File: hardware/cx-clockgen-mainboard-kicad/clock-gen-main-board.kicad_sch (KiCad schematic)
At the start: 19 parts, among them J1 Conn_01x03_Pin, J2 Conn_01x03_Pin, J3 Headswitch_SMA, J4 Conn_01x01_Pin, J5 Conn_01x01_Pin, J6 Conn_01x01_Pin, J7 Conn_01x01_Pin, J8 Conn_Coaxial, U1 Pico

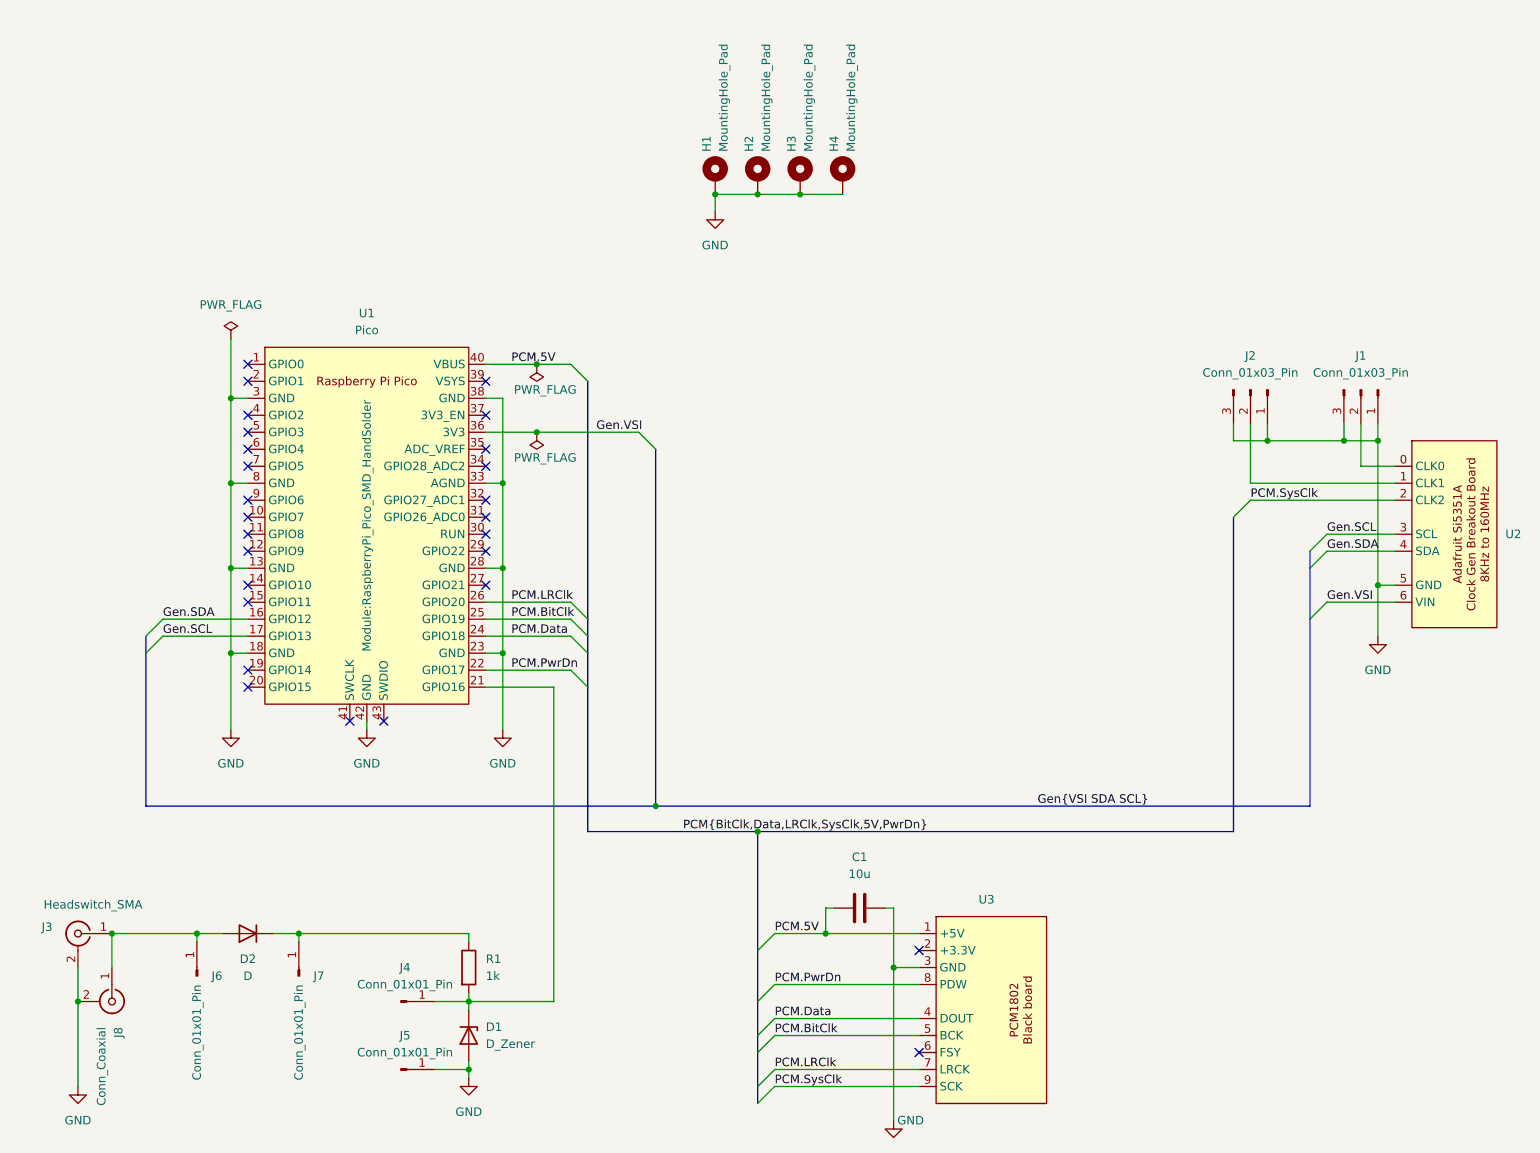
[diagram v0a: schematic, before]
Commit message: Added missing setup shell scripts
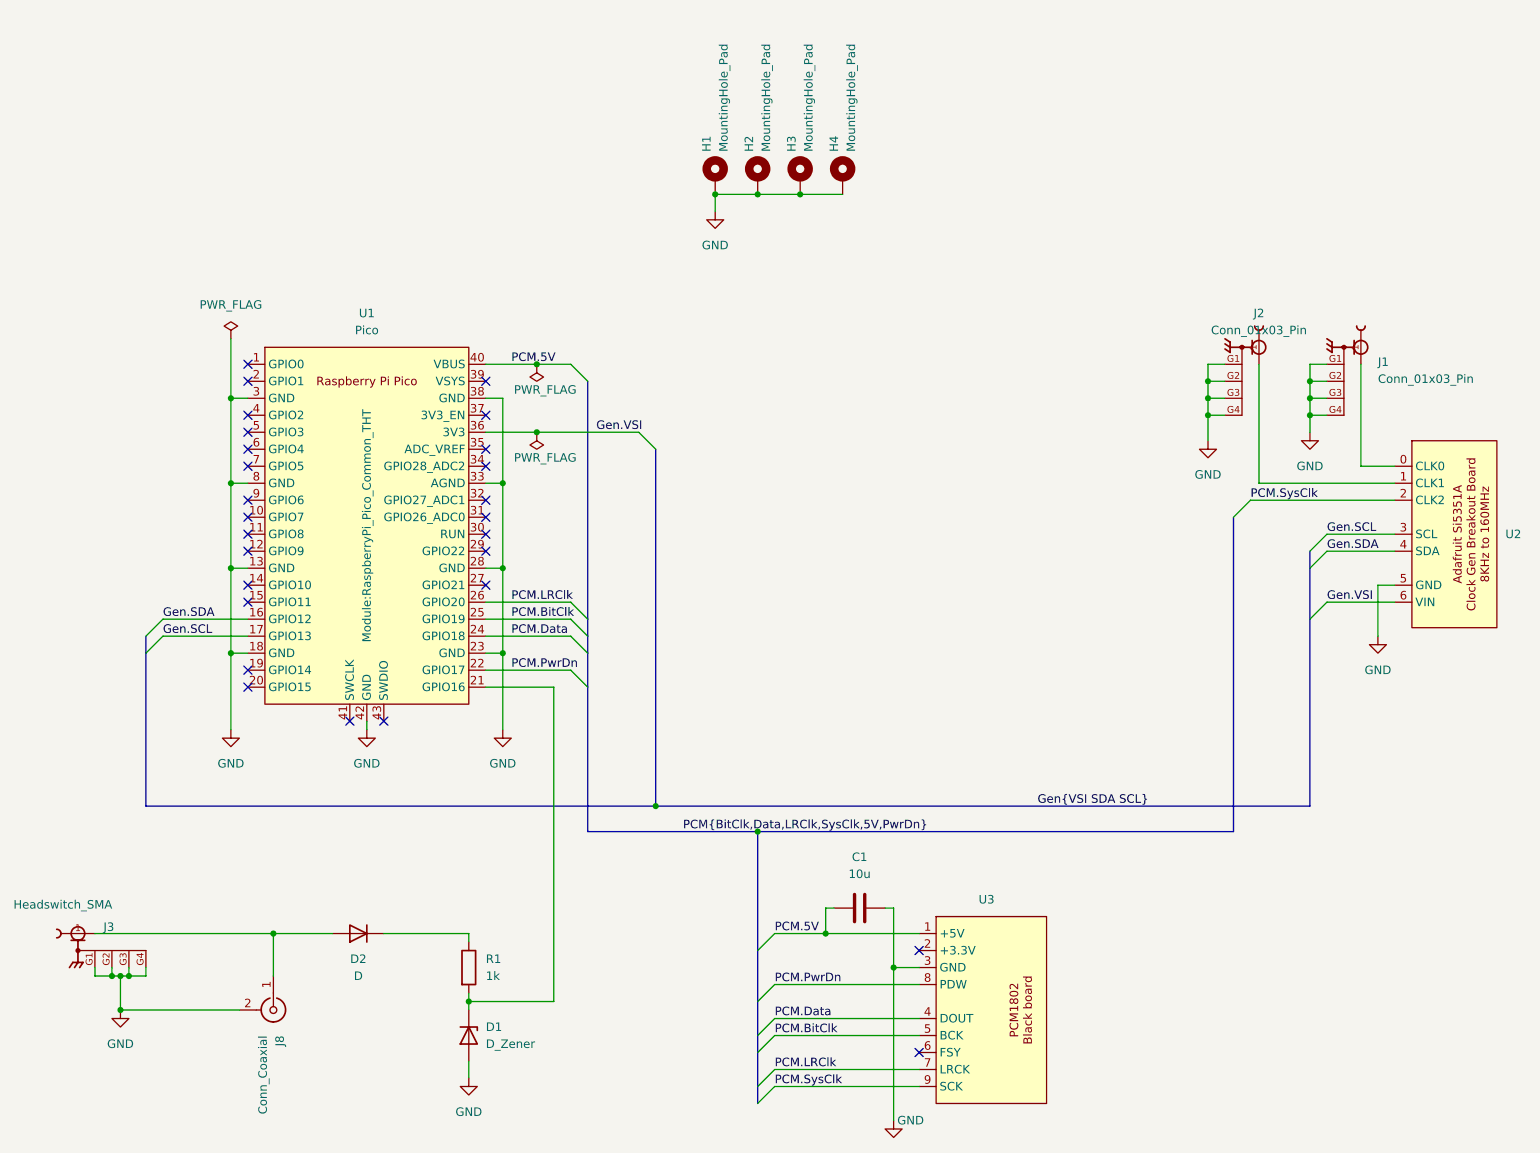
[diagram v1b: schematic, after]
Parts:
- removed J4, J5, J6, J7: Conn_01x01_Pin, Connector_PinHeader_2.54mm:PinHeader_1x01_P2.54mm_Vertical, symbol Connector:Conn_01x01_Pin
- J1, J2: footprint Connector_PinHeader_2.54mm:PinHeader_1x03_P2.54mm_Vertical -> Clockgen Footprints:GRADCONN_RFPC-SMA28-F; symbol Connector:Conn_01x03_Pin -> Clockgen Lib:RFPC-SMA28-F; MANUFACTURER (none) -> GradConn; MAXIMUM_PACKAGE_HEIGHT (none) -> 9.8mm; PARTREV (none) -> 1.0; STANDARD (none) -> Manufacturer Recommendations
- J3: footprint RFPC_SMA28_F:GRADCONN_RFPC-SMA28-F -> Clockgen Footprints:GRADCONN_RFPC-SMA28-F; symbol Connector:Conn_Coaxial -> Clockgen Lib:RFPC-SMA28-F; MANUFACTURER (none) -> GradConn; MAXIMUM_PACKAGE_HEIGHT (none) -> 9.8mm; PARTREV (none) -> 1.0; STANDARD (none) -> Manufacturer Recommendations
- U1: footprint Module:RaspberryPi_Pico_SMD_HandSolder -> Module:RaspberryPi_Pico_Common_THT
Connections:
- net GND: now also J1.G1, J1.G2, J1.G3, J1.G4, J2.G1, J2.G2, J2.G3, J2.G4, J3.G1, J3.G2, J3.G3, J3.G4; no longer J1.1 (Pin_1), J1.3 (Pin_3), J2.1 (Pin_1), J2.3 (Pin_3), J3.2 (Ext)
- net at U2.1 (CLK1): now also J2.1; no longer J2.2 (Pin_2)
- net at U2.0 (CLK0): now also J1.1; no longer J1.2 (Pin_2)
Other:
- moved on the sheet: D2, J8

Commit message: Updated build and installation scripts for improved functionality and error handling; added new package installation logic for Debian and Fedora, enhanced logging, and refined project settings in KiCad files. Also, added new entries to .gitignore and made minor adjustments to README.
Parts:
- U2, U3: value ~ -> (none)

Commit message: Remove obsolete KiCad library files, including symbol, footprint, and 3D model files for ADA4857-1YRZ-R7 and related components, to streamline project resources and eliminate unused assets.
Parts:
- J1, J2, J3: footprint Clockgen Footprints:GRADCONN_RFPC-SMA28-F -> GDH Connectors:GRADCONN_RFPC-SMA28-F; symbol Clockgen Lib:RFPC-SMA28-F -> GDH Connectors:RFPC-SMA28-F
- J8: footprint vhs_decode_footprints:Molex_0731000154_BNC_RA_THT -> GDH Connectors:Molex_0731000154_BNC_RA_THT
- U1: symbol MCU_RaspberryPi_and_Boards:Pico -> GDH Modules:Raspberry Pi Pico
- U2: footprint adafruit-si5351:Adafruit_Si5351A_Breakout_Board -> GDH Modules:Adafruit_Si5351A_Breakout_Board; symbol adafruit-si5351:Adafruit_Si5351A -> GDH Modules:Adafruit_Si5351A
- U3: footprint black-pcm1802:black-pcm1802-board -> GDH Modules:black-pcm1802-board; symbol black-pcm1802:black-pcm1802-board -> GDH Modules:black-pcm1802-board
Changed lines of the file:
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@@
 	)
 	(symbol
-		(lib_id "black-pcm1802:black-pcm1802-board")
+		(lib_id "GDH Modules:black-pcm1802-board")
 		(at 154.94 163.83 0)
 		(unit 1)
@@
 			)
 		)
-		(property "Footprint" "black-pcm1802:black-pcm1802-board"
+		(property "Footprint" "GDH Modules:black-pcm1802-board"
 			(at 147.32 167.64 0)
 			(hide yes)
@@
 	)
 	(symbol
-		(lib_id "Clockgen Lib:RFPC-SMA28-F")
+		(lib_id "GDH Connectors:RFPC-SMA28-F")
 		(at 195.58 64.77 270)
 		(unit 1)
@@
 			)
 		)
-		(property "Footprint" "Clockgen Footprints:GRADCONN_RFPC-SMA28-F"
+		(property "Footprint" "GDH Connectors:GRADCONN_RFPC-SMA28-F"
 			(at 195.58 64.77 0)
 			(hide yes)
@@
 	)
 	(symbol
-		(lib_id "adafruit-si5351:Adafruit_Si5351A")
+		(lib_id "GDH Modules:Adafruit_Si5351A")
 		(at 224.79 92.71 0)
 		(unit 1)
@@
 			)
 		)
-		(property "Footprint" "adafruit-si5351:Adafruit_Si5351A_Breakout_Board"
+		(property "Footprint" "GDH Modules:Adafruit_Si5351A_Breakout_Board"
 			(at 224.79 109.22 0)
 			(hide yes)
@@
 	)
 	(symbol
-		(lib_id "Clockgen Lib:RFPC-SMA28-F")
+		(lib_id "GDH Connectors:RFPC-SMA28-F")
 		(at 19.05 152.4 0)
 		(unit 1)
@@
 			)
 		)
-		(property "Footprint" "Clockgen Footprints:GRADCONN_RFPC-SMA28-F"
+		(property "Footprint" "GDH Connectors:GRADCONN_RFPC-SMA28-F"
 			(at 19.05 152.4 0)
 			(hide yes)
@@
 	)
 	(symbol
-		(lib_id "MCU_RaspberryPi_and_Boards:Pico")
+		(lib_id "GDH Modules:Raspberry Pi Pico")
 		(at 62.23 91.44 0)
 		(unit 1)
@@
 			)
 		)
-		(property "Footprint" "vhs_decode_footprints:Molex_0731000154_BNC_RA_THT"
+		(property "Footprint" "GDH Connectors:Molex_0731000154_BNC_RA_THT"
 			(at 48.26 163.83 0)
 			(hide yes)
@@
 	)
 	(symbol
-		(lib_id "Clockgen Lib:RFPC-SMA28-F")
+		(lib_id "GDH Connectors:RFPC-SMA28-F")
 		(at 210.82 64.77 270)
 		(unit 1)
@@
 			)
 		)
-		(property "Footprint" "Clockgen Footprints:GRADCONN_RFPC-SMA28-F"
+		(property "Footprint" "GDH Connectors:GRADCONN_RFPC-SMA28-F"
 			(at 210.82 64.77 0)
 			(hide yes)

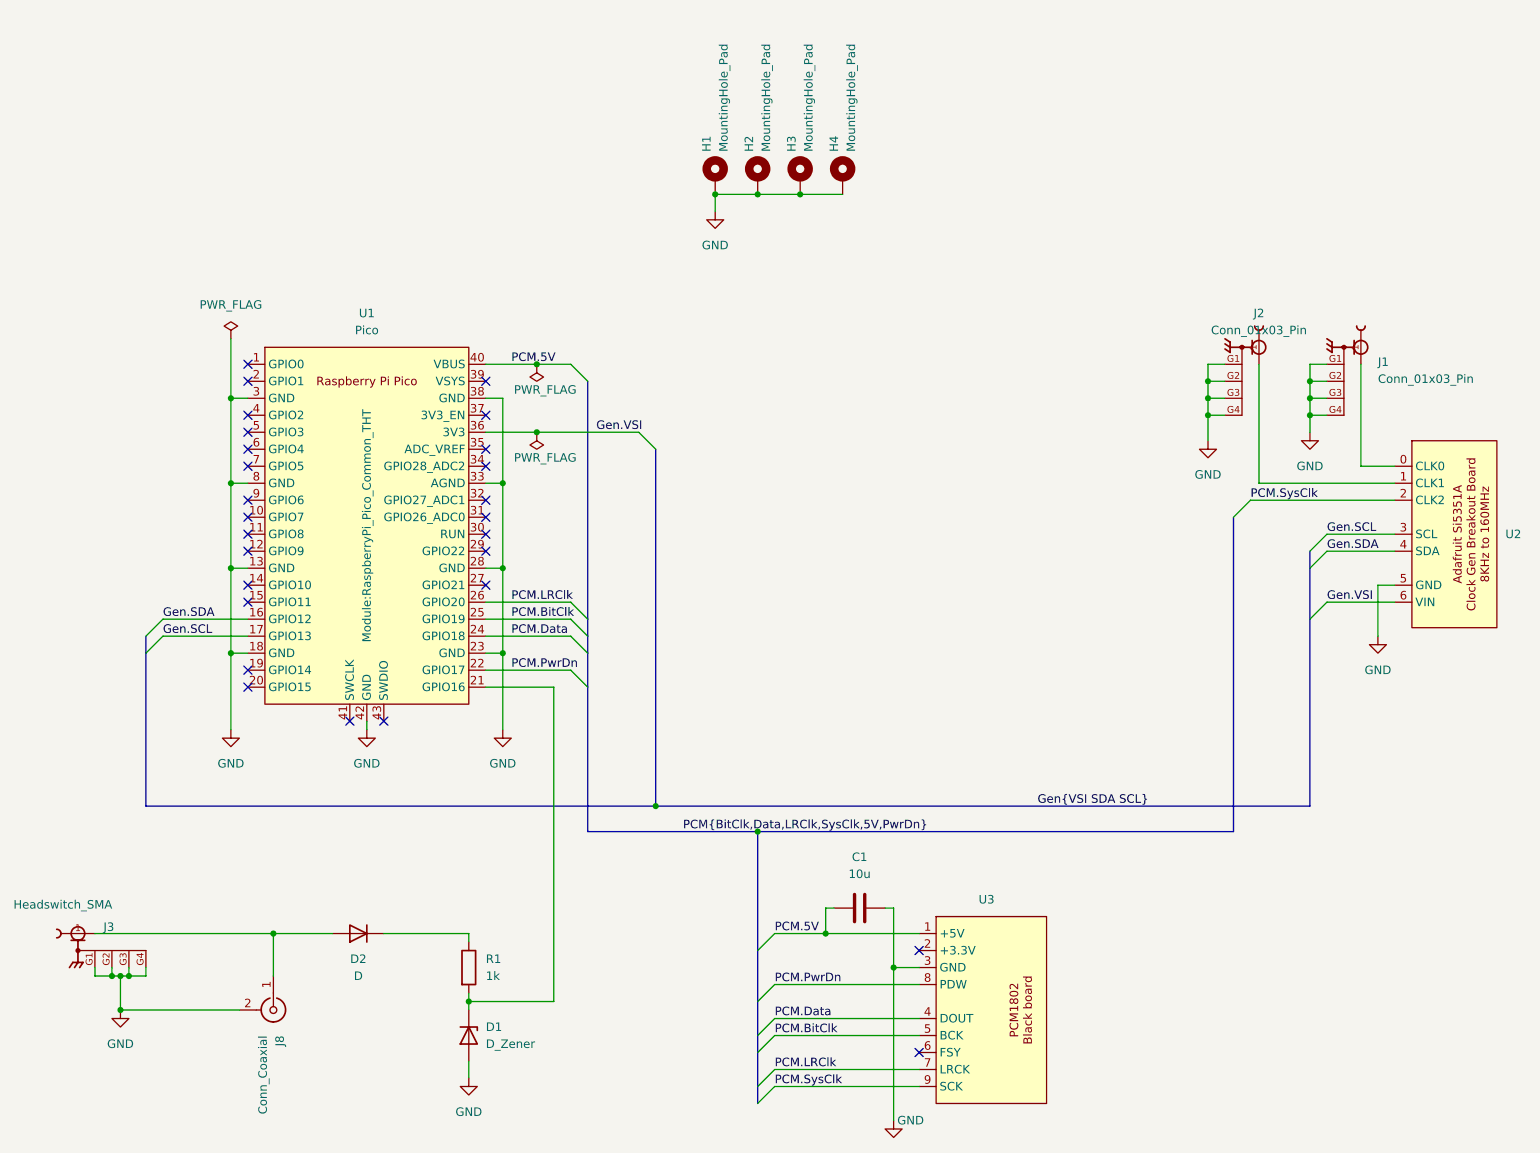
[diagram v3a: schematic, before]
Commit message: Update KiCad project files: modified project title and version, adjusted component properties, and streamlined pin functions for clarity. Removed obsolete library references and updated netlist handling for improved error management. Enhanced design parameters and added new connector symbols for better integration.
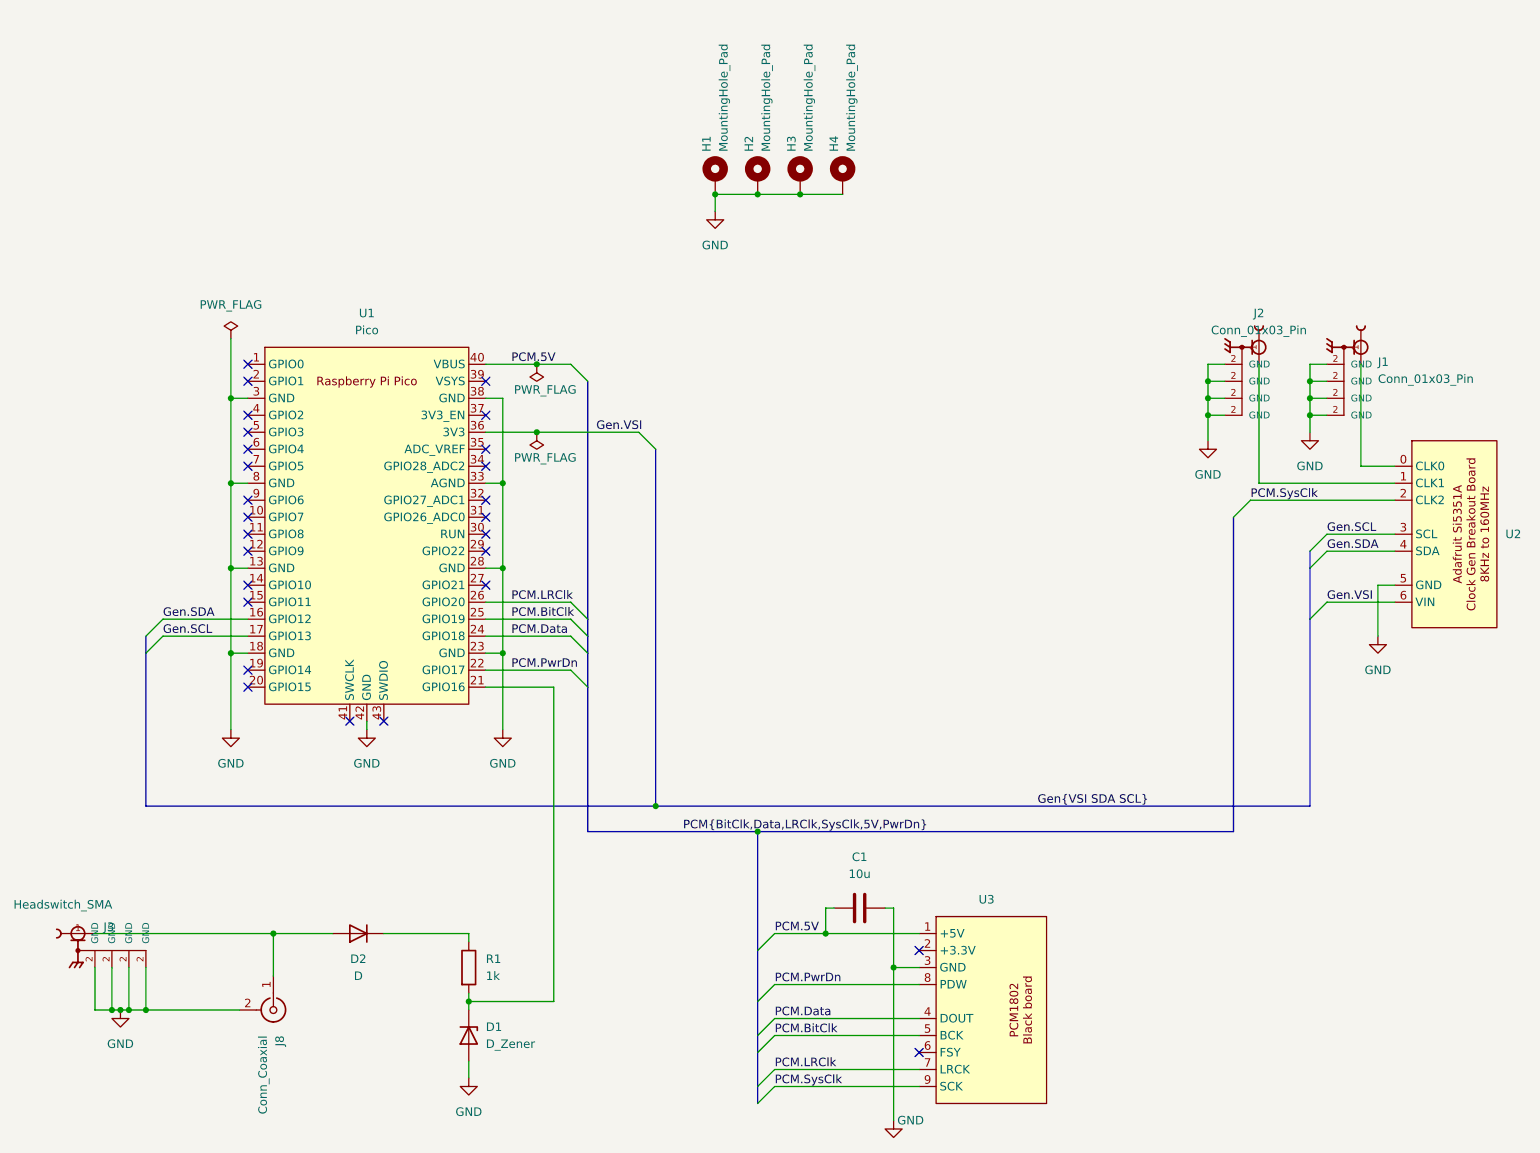
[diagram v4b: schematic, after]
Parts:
- J1, J2, J3: MPN (none) -> RFPC-SMA28-F; Manufacturer (none) -> GCT
- U1: footprint Module:RaspberryPi_Pico_Common_THT -> GDH Modules:Pi_Pico_SMD_TH; MPN (none) -> Raspberry Pi Pico; Manufacturer (none) -> Raspberry Pi
- U2: MPN (none) -> 2045; Manufacturer (none) -> Adafruit Industries
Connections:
- net GND: now also J1.2 (GND), J2.2 (GND), J3.2 (GND); no longer J1.G1, J1.G2, J1.G3, J1.G4, J2.G1, J2.G2, J2.G3, J2.G4, J3.G1, J3.G2, J3.G3, J3.G4
